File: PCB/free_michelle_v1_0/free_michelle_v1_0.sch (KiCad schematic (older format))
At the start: 3 parts

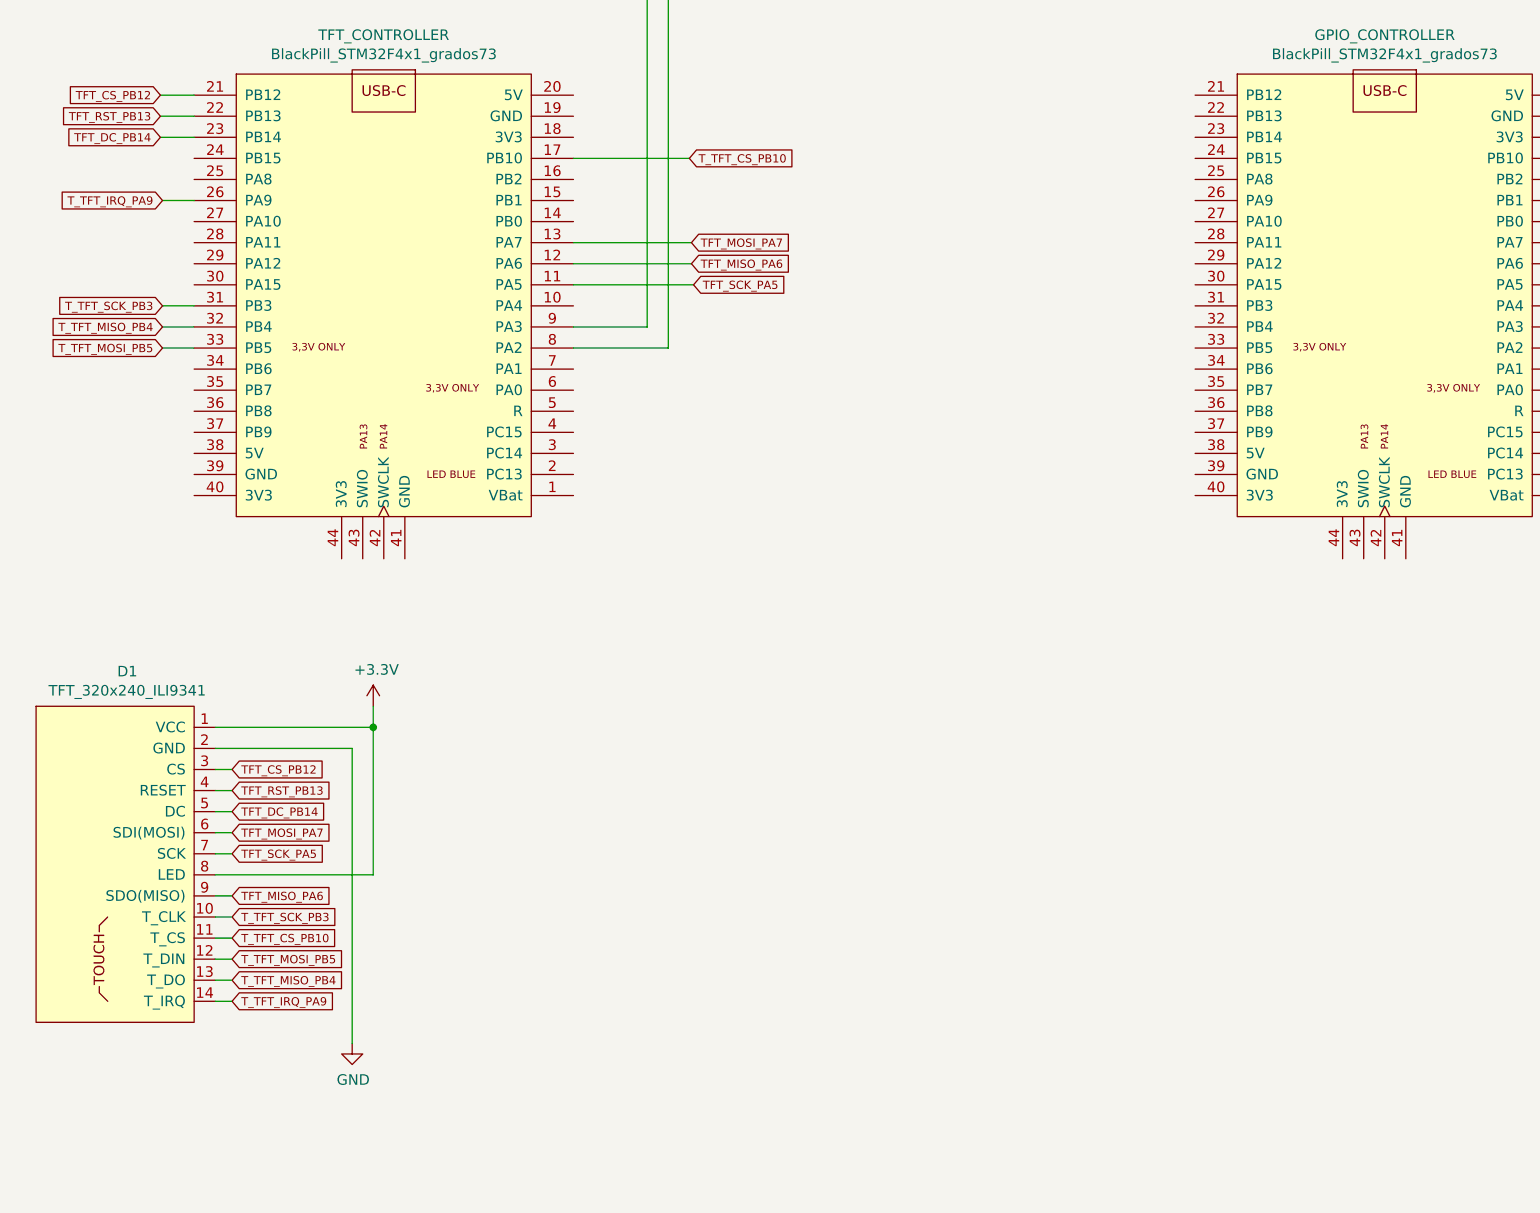
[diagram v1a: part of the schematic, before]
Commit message: Dodany DS3231 i podłączony
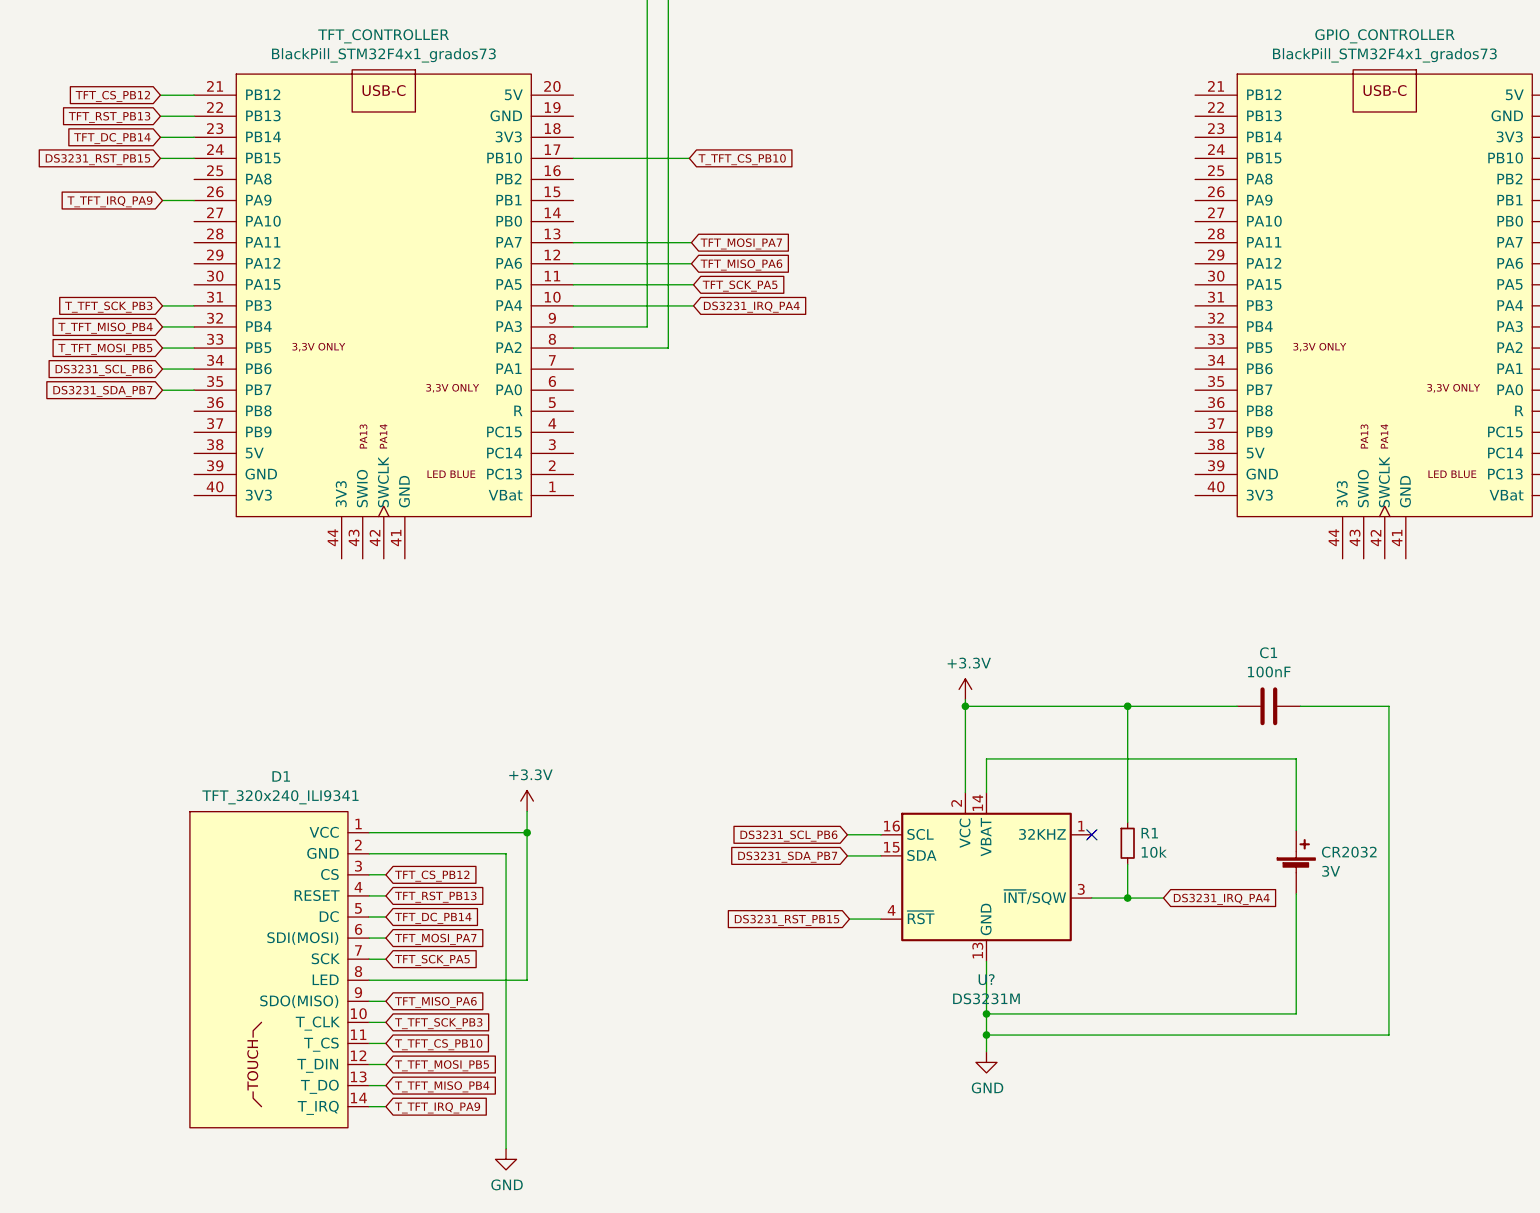
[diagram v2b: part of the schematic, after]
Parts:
- added C1: 100nF, symbol Device:C
- added CR2032: 3V, symbol Device:Battery_Cell
- added R1: 10k, symbol Device:R_Small
- added U?: DS3231M, Package_SO:SOIC-16W_7.5x10.3mm_P1.27mm, symbol Timer_RTC:DS3231M
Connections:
- net +3V3: now also C1.1, R1.1, U?.2 (VCC)
- net GND: now also C1.2, CR2032.2 (-), U?.10 (GND), U?.11 (GND), U?.12 (GND), U?.13 (GND), U?.5 (GND), U?.6 (GND), U?.7 (GND), U?.8 (GND), U?.9 (GND)
- net DS3231_IRQ_PA4: now reaches TFT_CONTROLLER.10 (PA4)
- net DS3231_IRQ_PA4: now also R1.2, U?.3 (~INT~/SQW)
- net DS3231_RST_PB15: now reaches TFT_CONTROLLER.24 (PB15)
- net DS3231_RST_PB15: now also U?.4 (~RST)
- net DS3231_SCL_PB6: now reaches TFT_CONTROLLER.34 (PB6)
- net DS3231_SCL_PB6: now also U?.16 (SCL)
- net DS3231_SDA_PB7: now reaches TFT_CONTROLLER.35 (PB7)
- net DS3231_SDA_PB7: now also U?.15 (SDA)
- new net: CR2032.1 (+), U?.14 (VBAT)
- no-connect marks 0 -> 1
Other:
- moved on the sheet: D1
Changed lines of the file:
@@
 L grad73_library:TFT_320x240_ILI9341 D1
 U 1 1 61DB7F28
-P 1700 4400
-F 0 "D1" H 1433 4465 50  0000 C CNN
-F 1 "TFT_320x240_ILI9341" H 1433 4374 50  0000 C CNN
-F 2 "" H 1700 4400 50  0001 C CNN
-F 3 "" H 1700 4400 50  0001 C CNN
-	1    1700 4400
+P 2430 4900
+F 0 "D1" H 2163 4965 50  0000 C CNN
+F 1 "TFT_320x240_ILI9341" H 2163 4874 50  0000 C CNN
+F 2 "" H 2430 4900 50  0001 C CNN
+F 3 "" H 2430 4900 50  0001 C CNN
+	1    2430 4900
 	1    0    0    -1
 $EndComp
@@
 L power:GND #PWR?
 U 1 1 61DBA788
-P 2500 6100
-F 0 "#PWR?" H 2500 5850 50  0001 C CNN
-F 1 "GND" H 2505 5927 50  0000 C CNN
-F 2 "" H 2500 6100 50  0001 C CNN
-F 3 "" H 2500 6100 50  0001 C CNN
-	1    2500 6100
+P 3230 6600
+F 0 "#PWR?" H 3230 6350 50  0001 C CNN
+F 1 "GND" H 3235 6427 50  0000 C CNN
+F 2 "" H 3230 6600 50  0001 C CNN
+F 3 "" H 3230 6600 50  0001 C CNN
+	1    3230 6600
 	1    0    0    -1
 $EndComp
@@
 L power:+3.3V #PWR?
 U 1 1 61DBE35F
-P 2600 4500
-F 0 "#PWR?" H 2600 4350 50  0001 C CNN
-F 1 "+3.3V" H 2615 4673 50  0000 C CNN
-F 2 "" H 2600 4500 50  0001 C CNN
-F 3 "" H 2600 4500 50  0001 C CNN
-	1    2600 4500
+P 3330 5000
+F 0 "#PWR?" H 3330 4850 50  0001 C CNN
+F 1 "+3.3V" H 3345 5173 50  0000 C CNN
+F 2 "" H 3330 5000 50  0001 C CNN
+F 3 "" H 3330 5000 50  0001 C CNN
+	1    3330 5000
 	1    0    0    -1
 $EndComp
@@
 Wire Wire Line
 	13870 1060 13870 1140
-Text GLabel 1930 4800 2    39   Input ~ 0
+Text GLabel 2660 5300 2    39   Input ~ 0
 TFT_CS_PB12
 Text GLabel 1590 1600 0    39   Input ~ 0
@@
 	1590 1600 1750 1600
 Wire Wire Line
-	1850 4800 1930 4800
-Text GLabel 1930 4900 2    39   Input ~ 0
+	2580 5300 2660 5300
+Text GLabel 2660 5400 2    39   Input ~ 0
 TFT_RST_PB13
 Wire Wire Line
-	1850 4900 1930 4900
+	2580 5400 2660 5400
 Text GLabel 1590 1700 0    39   Input ~ 0
 TFT_RST_PB13
 Wire Wire Line
 	1590 1700 1750 1700
-Text GLabel 1930 5000 2    39   Input ~ 0
+Text GLabel 2660 5500 2    39   Input ~ 0
 TFT_DC_PB14
 Wire Wire Line
-	1930 5000 1850 5000
+	2660 5500 2580 5500
 Text GLabel 1590 1800 0    39   Input ~ 0
 TFT_DC_PB14
 Wire Wire Line
 	1590 1800 1750 1800
-Text GLabel 1930 5100 2    39   Input ~ 0
+Text GLabel 2660 5600 2    39   Input ~ 0
 TFT_MOSI_PA7
 Wire Wire Line
-	1930 5100 1850 5100
-Text GLabel 1930 5200 2    39   Input ~ 0
+	2660 5600 2580 5600
+Text GLabel 2660 5700 2    39   Input ~ 0
 TFT_SCK_PA5
 Wire Wire Line
-	1930 5200 1850 5200
+	2660 5700 2580 5700
 Text GLabel 4110 2300 2    39   Input ~ 0
 TFT_MOSI_PA7
@@
 	4120 2500 3550 2500
 Wire Wire Line
-	1850 4600 2600 4600
-Wire Wire Line
-	2600 4600 2600 4500
-Wire Wire Line
-	1850 5300 2600 5300
-Wire Wire Line
-	2600 5300 2600 4600
-Connection ~ 2600 4600
-Text GLabel 1930 5400 2    39   Input ~ 0
+	2580 5100 3330 5100
+Wire Wire Line
+	3330 5100 3330 5000
+Wire Wire Line
+	2580 5800 3330 5800
+Wire Wire Line
+	3330 5800 3330 5100
+Connection ~ 3330 5100
+Text GLabel 2660 5900 2    39   Input ~ 0
 TFT_MISO_PA6
 Wire Wire Line
-	1930 5400 1850 5400
+	2660 5900 2580 5900
 Text GLabel 4110 2400 2    39   Input ~ 0
 TFT_MISO_PA6
 Wire Wire Line
 	4110 2400 3550 2400
-Text GLabel 1930 5500 2    39   Input ~ 0
+Text GLabel 2660 6000 2    39   Input ~ 0
 T_TFT_SCK_PB3
 Wire Wire Line
-	1930 5500 1850 5500
-Text GLabel 1930 5600 2    39   Input ~ 0
+	2660 6000 2580 6000
+Text GLabel 2660 6100 2    39   Input ~ 0
 T_TFT_CS_PB10
-Text GLabel 1930 5700 2    39   Input ~ 0
+Text GLabel 2660 6200 2    39   Input ~ 0
 T_TFT_MOSI_PB5
-Text GLabel 1930 5800 2    39   Input ~ 0
+Text GLabel 2660 6300 2    39   Input ~ 0
 T_TFT_MISO_PB4
-Text GLabel 1930 5900 2    39   Input ~ 0
+Text GLabel 2660 6400 2    39   Input ~ 0
 T_TFT_IRQ_PA9
 Wire Wire Line
-	1930 5600 1850 5600
-Wire Wire Line
-	1930 5700 1850 5700
-Wire Wire Line
-	1930 5800 1850 5800
-Wire Wire Line
-	1930 5900 1850 5900
+	2660 6100 2580 6100
+Wire Wire Line
+	2660 6200 2580 6200
+Wire Wire Line
+	2660 6300 2580 6300
+Wire Wire Line
+	2660 6400 2580 6400
 Text GLabel 1600 2600 0    39   Input ~ 0
 T_TFT_SCK_PB3
@@
 	4100 1900 3550 1900
 Wire Wire Line
-	2500 6100 2500 4700
-Wire Wire Line
-	2500 4700 1850 4700
+	3230 6600 3230 5200
+Wire Wire Line
+	3230 5200 2580 5200
+$Comp
+L Timer_RTC:DS3231M U?
+U 1 1 61DE62B5
+P 5510 5310
+F 0 "U?" H 5510 4821 50  0000 C CNN
+F 1 "DS3231M" H 5510 4730 50  0000 C CNN
+F 2 "Package_SO:SOIC-16W_7.5x10.3mm_P1.27mm" H 5510 4710 50  0001 C CNN
+F 3 "http://datasheets.maximintegrated.com/en/ds/DS3231.pdf" H 5780 5360 50  0001 C CNN
+	1    5510 5310
+	1    0    0    -1
+$EndComp
+NoConn ~ 6010 5110
+Text GLabel 4850 5110 0    39   Input ~ 0
+DS3231_SCL_PB6
+Text GLabel 1600 2900 0    39   Input ~ 0
+DS3231_SCL_PB6
+Wire Wire Line
+	1600 2900 1750 2900
+Wire Wire Line
+	4850 5110 5010 5110
+Text GLabel 4850 5210 0    39   Input ~ 0
+DS3231_SDA_PB7
+Wire Wire Line
+	4850 5210 5010 5210
+Text GLabel 1600 3000 0    39   Input ~ 0
+DS3231_SDA_PB7
+Wire Wire Line
+	1600 3000 1750 3000
+Text GLabel 4120 2600 2    39   Input ~ 0
+DS3231_IRQ_PA4
+Wire Wire Line
+	4120 2600 3550 2600
+$Comp
+L power:+3.3V #PWR?
+U 1 1 61DEE9A8
+P 5410 4470
+F 0 "#PWR?" H 5410 4320 50  0001 C CNN
+F 1 "+3.3V" H 5425 4643 50  0000 C CNN
+F 2 "" H 5410 4470 50  0001 C CNN
+F 3 "" H 5410 4470 50  0001 C CNN
+	1    5410 4470
+	1    0    0    -1
+$EndComp
+$Comp
+L power:GND #PWR?
+U 1 1 61DF0A08
+P 5510 6140
+F 0 "#PWR?" H 5510 5890 50  0001 C CNN
+F 1 "GND" H 5515 5967 50  0000 C CNN
+F 2 "" H 5510 6140 50  0001 C CNN
+F 3 "" H 5510 6140 50  0001 C CNN
+	1    5510 6140
+	1    0    0    -1
+$EndComp
+$Comp
+L Device:Battery_Cell CR2032
+U 1 1 61DF2F26
+P 6980 5290
+F 0 "CR2032" H 7098 5386 50  0000 L CNN
+F 1 "3V" H 7098 5295 50  0000 L CNN
+F 2 "" V 6980 5350 50  0001 C CNN
+F 3 "~" V 6980 5350 50  0001 C CNN
+	1    6980 5290
+	1    0    0    -1
+$EndComp
+Wire Wire Line
+	6980 5090 6980 4750
+Wire Wire Line
+	6980 4750 5510 4750
+Wire Wire Line
+	5510 4750 5510 4910
+Wire Wire Line
+	6980 5390 6980 5960
+Wire Wire Line
+	6980 5960 5510 5960
+Connection ~ 5510 5960
+Wire Wire Line
+	5510 5960 5510 5710
+Text GLabel 6350 5410 2    39   Input ~ 0
+DS3231_IRQ_PA4
+Wire Wire Line
+	6010 5410 6180 5410
+Wire Wire Line
+	5410 4470 5410 4500
+$Comp
+L Device:R_Small R1
+U 1 1 61DFE4B3
+P 6180 5150
+F 0 "R1" H 6239 5196 50  0000 L CNN
+F 1 "10k" H 6239 5105 50  0000 L CNN
+F 2 "" H 6180 5150 50  0001 C CNN
+F 3 "~" H 6180 5150 50  0001 C CNN
+	1    6180 5150
+	1    0    0    -1
+$EndComp
+Wire Wire Line
+	6180 5250 6180 5410
+Connection ~ 6180 5410
+Wire Wire Line
+	6180 5410 6350 5410
+Wire Wire Line
+	6180 5050 6180 4500
+Wire Wire Line
+	6180 4500 5410 4500
+Connection ~ 5410 4500
+Wire Wire Line
+	5410 4500 5410 4910
+Wire Wire Line
+	5510 5960 5510 6060
+Wire Wire Line
+	7420 4500 7420 6060
+Wire Wire Line
+	7420 6060 5510 6060
+Connection ~ 5510 6060
+Wire Wire Line
+	5510 6060 5510 6140
+$Comp
+L Device:C C1
+U 1 1 61E06AF8
+P 6850 4500
+F 0 "C1" V 7102 4500 50  0000 C CNN
+F 1 "100nF" V 7011 4500 50  0000 C CNN
+F 2 "" H 6888 4350 50  0001 C CNN
+F 3 "~" H 6850 4500 50  0001 C CNN
+	1    6850 4500
+	0    -1   -1   0
+$EndComp
+Wire Wire Line
+	6180 4500 6700 4500
+Connection ~ 6180 4500
+Wire Wire Line
+	7000 4500 7420 4500
+Text GLabel 4860 5510 0    39   Input ~ 0
+DS3231_RST_PB15
+Wire Wire Line
+	4860 5510 5010 5510
+Text GLabel 1590 1900 0    39   Input ~ 0
+DS3231_RST_PB15
+Wire Wire Line
+	1590 1900 1750 1900
 $EndSCHEMATC
